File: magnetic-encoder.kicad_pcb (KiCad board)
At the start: 4 copper layers, 45.9 x 45.9 mm, 11 parts, among them J1 8P8C, U1 PCA9615, U2 AS5048B

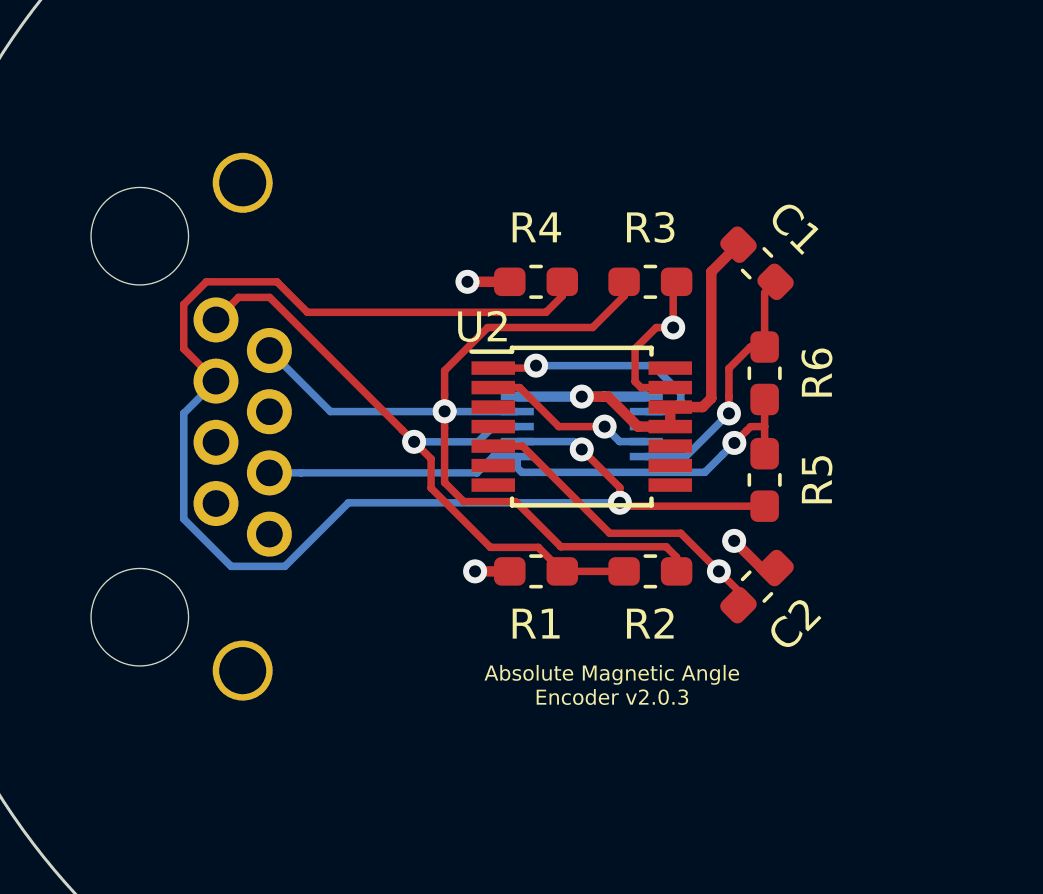
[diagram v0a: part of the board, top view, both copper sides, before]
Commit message: Fix differential tracing
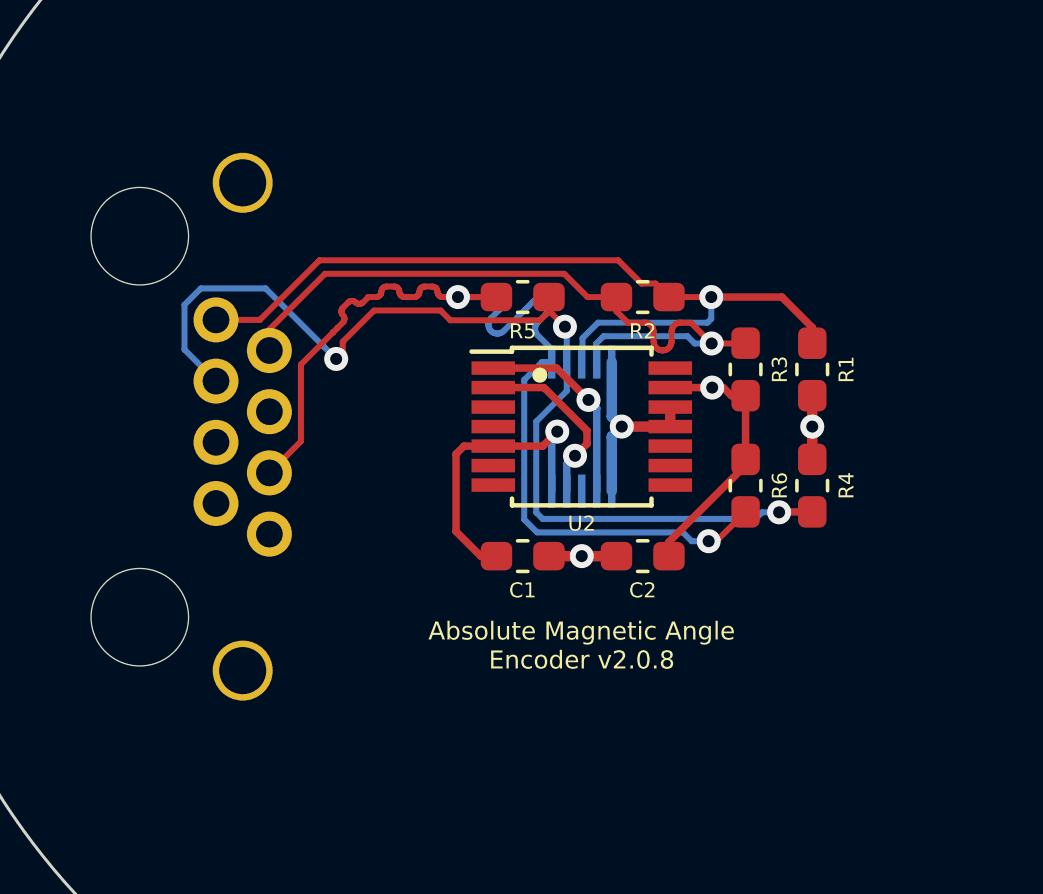
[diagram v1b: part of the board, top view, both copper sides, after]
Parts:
- moved C1 12.5 mm to (226.1, 138.4), turned to 180 degrees
- moved R4 11.4 mm to (235.8, 136.1), turned to 90 degrees
- moved R1 11.4 mm to (235.8, 132.2), turned to 270 degrees
- moved R5 10.1 mm to (226.1, 129.8), turned to 0 degrees
- moved R2 9.15 mm to (230.1, 129.8), turned to 0 degrees
- moved R3 4.31 mm to (233.6, 132.2), turned to 90 degrees
- moved C2 3.94 mm to (230.1, 138.4), turned to 180 degrees
- moved R6 3.80 mm to (233.6, 136.1)
- turned U1 to 90 degrees
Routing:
- net GND: track 80.4 -> 62.0 mm, vias 3 -> 2
- net +3V3: track 54.7 -> 37.4 mm, vias 4 -> 3
- net DSCL-: track 19.9 -> 34.5 mm, vias 1 -> 2
- net DSCL+: track 47.6 -> 35.2 mm, vias 2 -> 3
- net DSDA+: track 21.9 -> 28.2 mm
- net DSDA-: track 29.6 -> 24.7 mm
- net Net-(U1-Pad2): track 8.22 -> 6.77 mm
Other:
- board text added: "Absolute Magnetic Angle Encoder v2.0.8"
- board text removed: "Absolute Magnetic Angle Encoder v2.0.3"

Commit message: Add cat5e shielding
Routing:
- net GND: track 62.0 -> 26.0 mm, vias 2 -> 1
- net +3V3: track 37.4 -> 16.0 mm, vias 3 -> 2
- added copper zone on In2.Cu, net +3V3
- added copper zone on In1.Cu, net GND
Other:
- board text added: "Absolute Magnetic Angle Encoder v2.0.9"
- board text removed: "Absolute Magnetic Angle Encoder v2.0.8"
